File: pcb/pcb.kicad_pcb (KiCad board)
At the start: 2 copper layers, 284.6 x 110.1 mm, 175 parts, among them J1 USB_C_Receptacle_USB2.0, J2 USB_C_Receptacle_USB2.0, J4 USB_C_Receptacle_USB2.0, J5 USB_C_Receptacle_USB2.0, SW1 SW_Push, U1 SL2.1A, U2 NCP1117-3.3_SOT223, U3 W25Q128JVS, U4 RP2040, Y1 ABM8-272-T3

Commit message: Redesign
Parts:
- removed the REF** at (228.1, 109.4)
- removed the REF** at (231.7, 207.0)
- removed the REF** at (365.0, 109.4)
- removed the REF** at (88.8, 211.8)
- removed the REF** at (365.6, 211.8)
- removed the REF** at (88.8, 108.8)
- added H1: MountingHole, MountingHole:MountingHole_2.1mm, F.Cu at (88.8, 108.8)
- added H2: MountingHole, MountingHole:MountingHole_2.1mm, F.Cu at (228.1, 109.4)
- added H3: MountingHole, MountingHole:MountingHole_2.1mm, F.Cu at (365.0, 109.4)
- added H4: MountingHole, MountingHole:MountingHole_2.1mm, F.Cu at (88.8, 211.8)
- added H5: MountingHole, MountingHole:MountingHole_2.1mm, F.Cu at (231.7, 207.0)
- added H6: MountingHole, MountingHole:MountingHole_2.1mm, F.Cu at (365.6, 211.8)
- S1, S10, S11, S12, S13, S14, S15, S16, S17, S18, S19, S2, S20, S21, S22, S23, S24, S25, S26, S27, S28, S29, S3, S30, S31, S32, S33, S37, S38, S39, S40, S41, S45, S47, S49, S5, S51, S53, S55, S56, S57, S59, S6, S61, S63, S8, S9: footprint ScottoKeebs_MX:MX_PCB_1.00u -> Switch_Keyboard_Hotswap_Kailh:SW_Hotswap_Kailh_MX_1.00u
- S4, S7: footprint ScottoKeebs_MX:MX_PCB_1.50u -> Switch_Keyboard_Hotswap_Kailh:SW_Hotswap_Kailh_MX_1.00u
- S42: footprint ScottoKeebs_MX:MX_PCB_2.25u -> Switch_Keyboard_Hotswap_Kailh:SW_Hotswap_Kailh_MX_2.25u
- S43: footprint ScottoKeebs_MX:MX_PCB_2.00u -> Switch_Keyboard_Hotswap_Kailh:SW_Hotswap_Kailh_MX_2.00u
- S44, S46, S48, S52, S54, S58, S72: footprint ScottoKeebs_MX:MX_PCB_1.25u -> Switch_Keyboard_Hotswap_Kailh:SW_Hotswap_Kailh_MX_1.25u
- S50: footprint ScottoKeebs_MX:MX_PCB_6.25u -> Switch_Keyboard_Hotswap_Kailh:SW_Hotswap_Kailh_MX_6.25u
- S67: footprint ScottoKeebs_MX:MX_PCB_2.75u -> Switch_Keyboard_Hotswap_Kailh:SW_Hotswap_Kailh_MX_2.75u
- S71: footprint ScottoKeebs_MX:MX_PCB_1.75u -> Switch_Keyboard_Hotswap_Kailh:SW_Hotswap_Kailh_MX_1.75u
- moved D50 1.19 mm to (225.6, 204.0)
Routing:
- net col5: track 293.7 -> 318.8 mm, vias 3 -> 9
- net col7: track 372.1 -> 393.0 mm, vias 1 -> 9
- net col9: track 365.2 -> 382.6 mm, vias 1 -> 5
- net col10: track 348.8 -> 366.3 mm, vias 1 -> 5
- net col8: track 382.4 -> 399.3 mm, vias 1 -> 5
- net col11: track 336.8 -> 352.1 mm, vias 1 -> 5
- net Net-(D71-A): track 16.0 -> 30.8 mm
- net col4: track 229.9 -> 243.8 mm, vias 1 -> 8
- net col3: track 162.0 -> 173.3 mm, vias 1 -> 9
- net col1: track 238.3 -> 248.4 mm, vias 1 -> 10
- net Net-(D42-A): track 15.1 -> 24.4 mm
- net /QSPI_SD3: track 143.3 -> 152.5 mm
- net col6: track 347.0 -> 356.1 mm, vias 1 -> 9
- net col12: track 323.6 -> 332.0 mm, vias 1 -> 4
- net /XOUT: track 138.9 -> 146.9 mm
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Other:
- board text added: "Made By Ronit D'Silva @CherryTree56567"

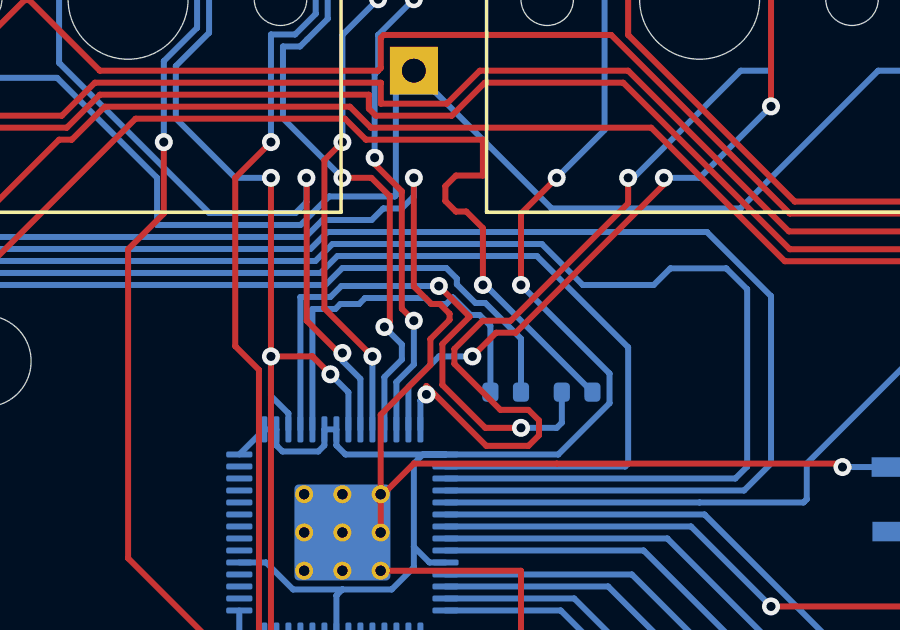
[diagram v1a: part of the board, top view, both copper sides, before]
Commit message: Fixed 3D Case and noise
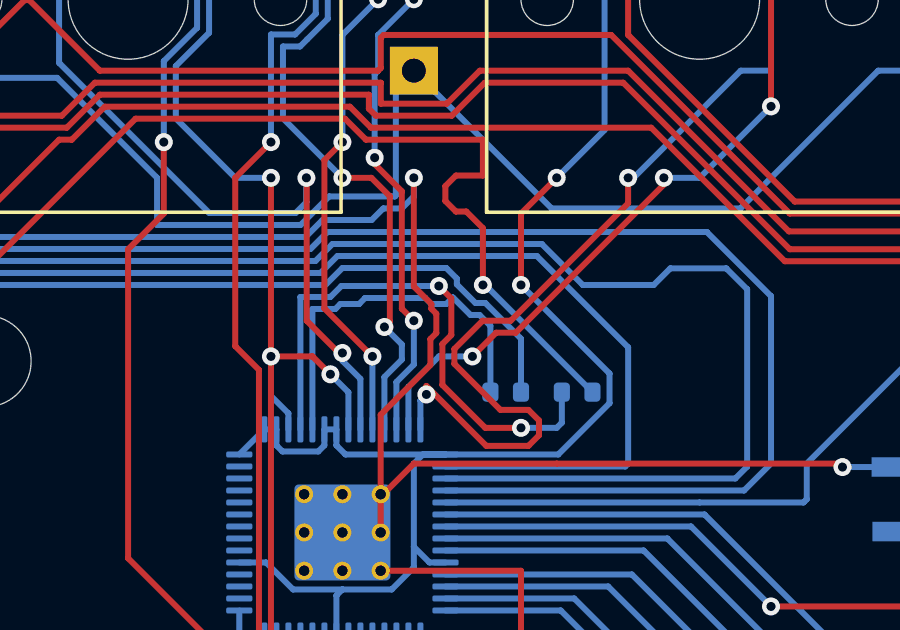
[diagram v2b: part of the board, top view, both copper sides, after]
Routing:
- net USBC_GND: track 599.3 -> 598.8 mm
- net Net-(U4-USB_DM): track 18.9 -> 18.4 mm
- added copper zone on B.Cu, net USBC_GND
- added copper zone on F.Cu, net USBC_GND
- removed copper zone on B.Cu, net (none)
- removed copper zone on F.Cu, net (none)
